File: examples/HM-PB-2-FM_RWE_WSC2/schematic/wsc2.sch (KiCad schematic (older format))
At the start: 32 parts, among them IC1 ATmega328P-MU, IC2 AT24C32, T1 BC856, T2 BC856, T3 NPN

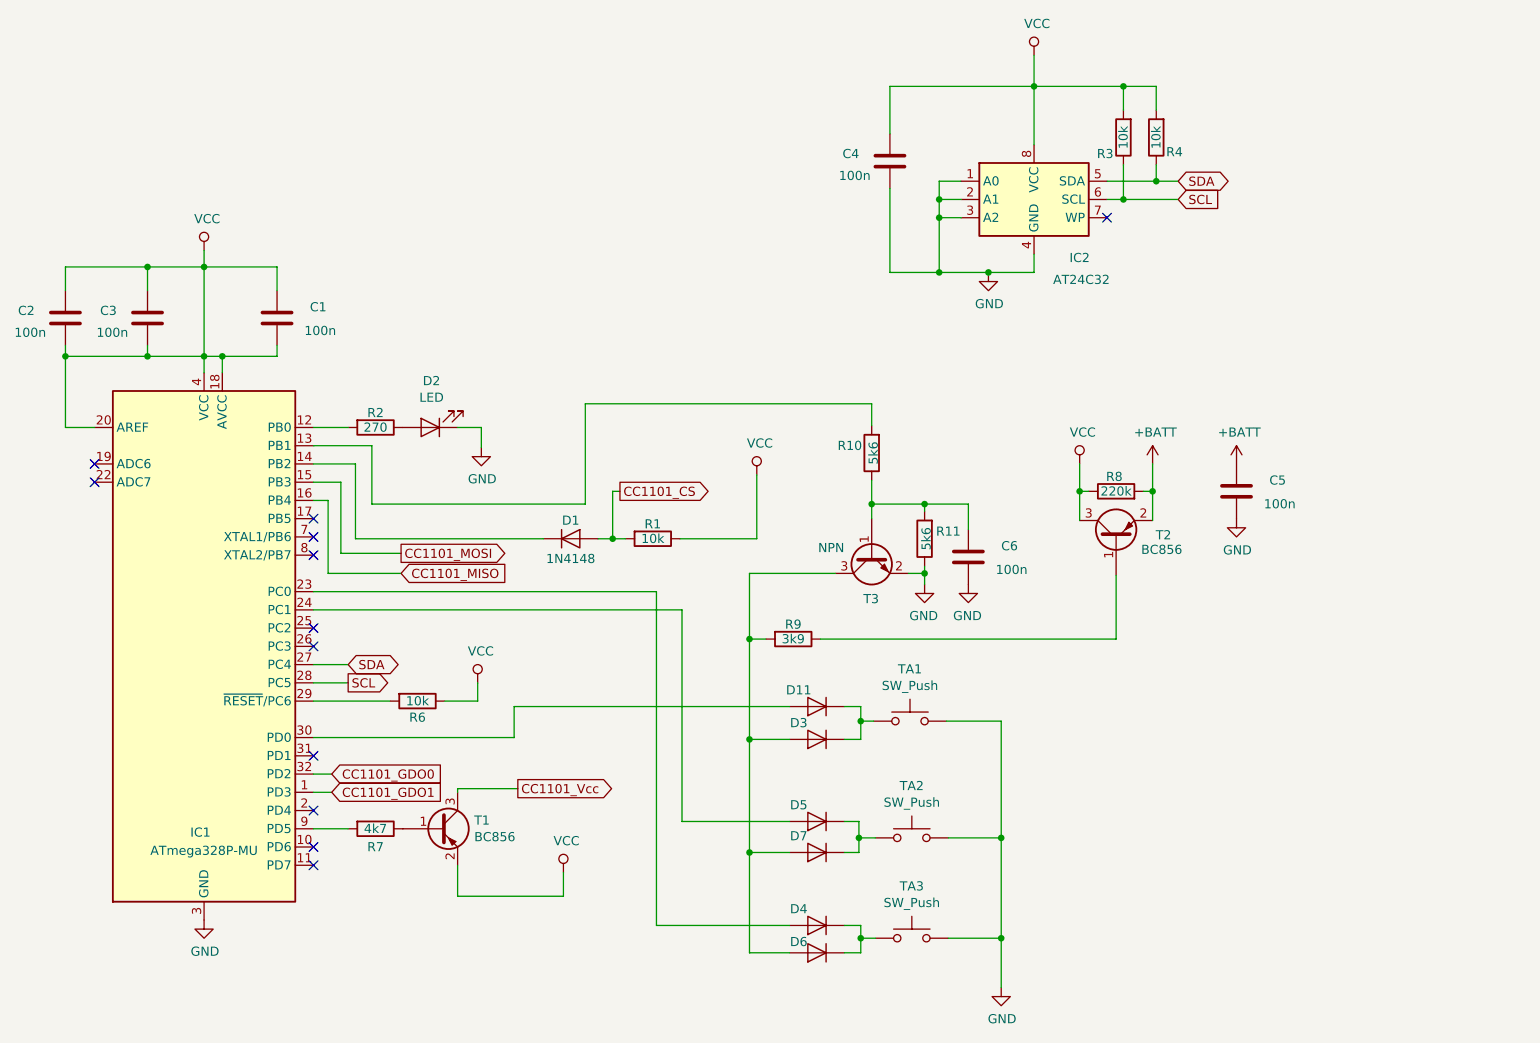
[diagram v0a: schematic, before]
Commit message: add schematic
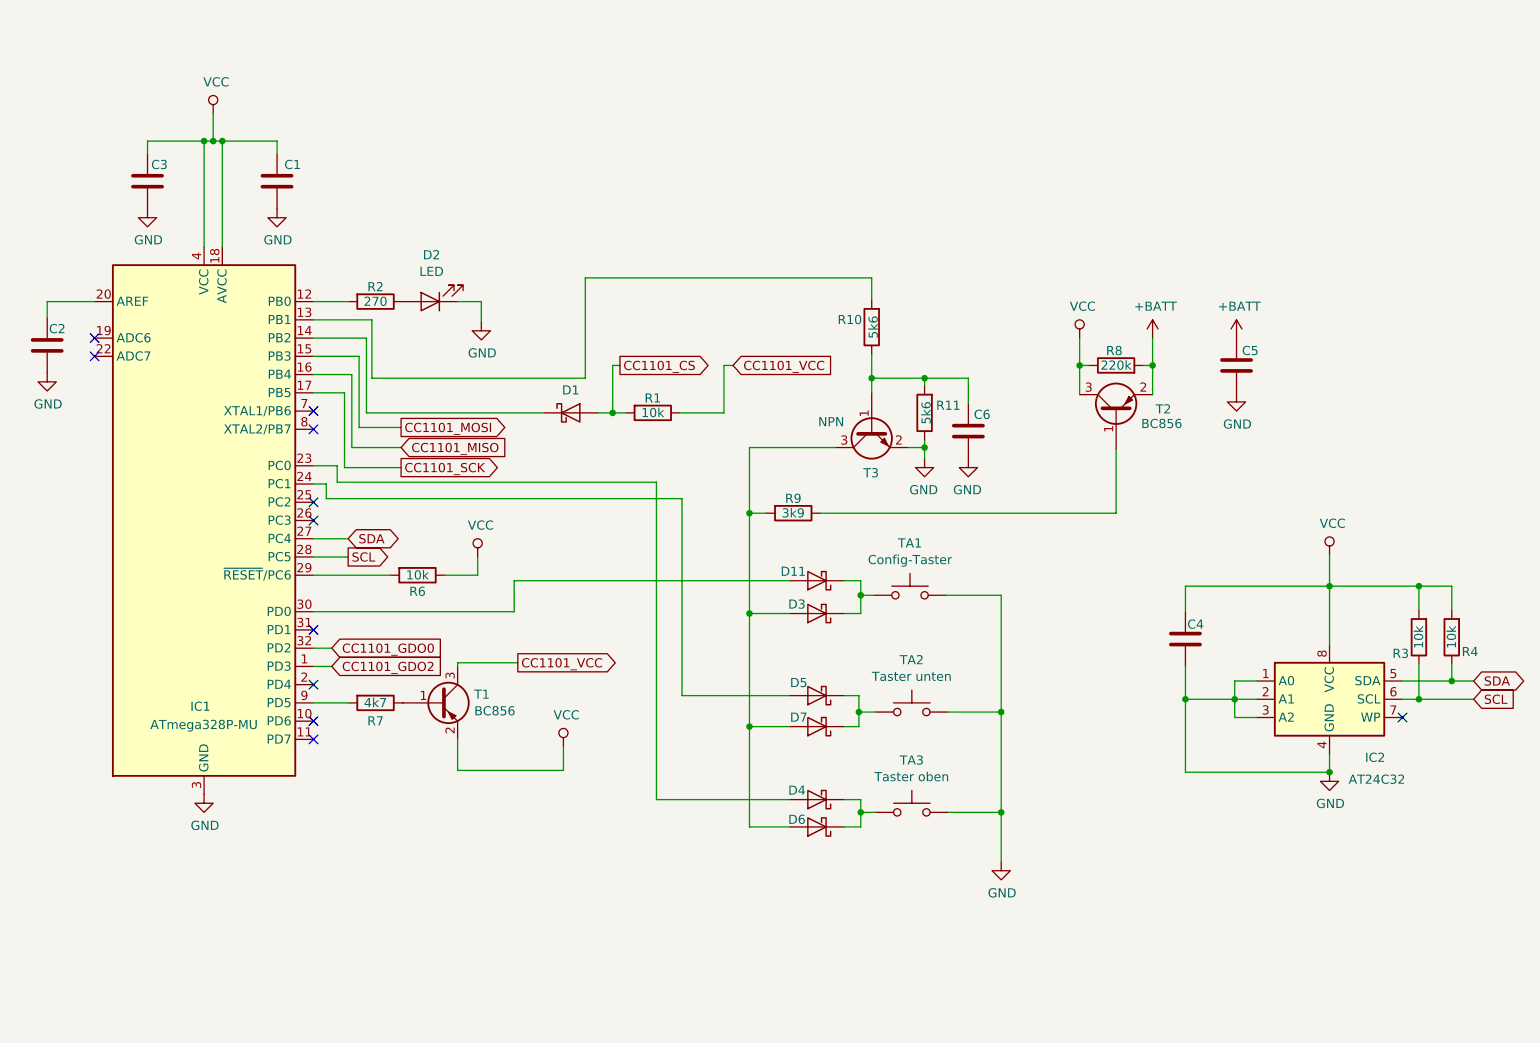
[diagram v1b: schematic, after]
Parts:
- removed D1: 1N4148, Diode_THT:D_DO-35_SOD27_P7.62mm_Horizontal, symbol Diode:1N4148
- removed D11, D3, D4, D5, D6, D7: D, symbol Device:D
- added D1, D11, D3, D4, D5, D6, D7: D_Schottky, symbol Device:D_Schottky
- TA1: value SW_Push -> Config-Taster
- TA2: value SW_Push -> Taster unten
- TA3: value SW_Push -> Taster oben
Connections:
- net CC1101_CS: now also D1.2 (A)
- net GND: now also C1.1, C2.1, C3.1
- net VCC: no longer C1.1, C2.1, C2.2, C3.1, IC1.20 (AREF), R1.1
- net at IC1.14 (PB2): now also D1.1 (K)
- net CC1101_SCK: now reaches IC1.17 (PB5)
- net at IC1.23 (PC0): now also D4.2 (A)
- net at IC1.24 (PC1): now also D5.2 (A)
- net at IC1.30 (PD0): now also D11.2 (A)
- net at TA1.1: now also D11.1 (K), D3.1 (K)
- net at TA2.1: now also D5.1 (K), D7.1 (K)
- net at TA3.1: now also D4.1 (K), D6.1 (K)
- net at R9.2, T3.3 (C): now also D3.2 (A), D6.2 (A), D7.2 (A)
- net CC1101_GDO1 renamed CC1101_GDO2
- net CC1101_Vcc renamed CC1101_VCC
- net CC1101_VCC: now also R1.1
- new net: C2.2, IC1.20 (AREF)
- no-connect marks 12 -> 11
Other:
- moved on the sheet: C1, C2, C3, C4, C5, C6, D2, IC1, IC2, R1, R10, R11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
